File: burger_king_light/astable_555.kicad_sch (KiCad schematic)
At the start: 2 parts, among them U1 ICM7555CBAZ

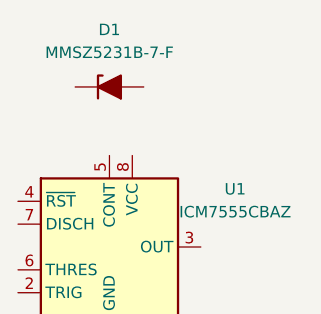
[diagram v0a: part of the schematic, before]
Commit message: changed diode designator from D1 to D2
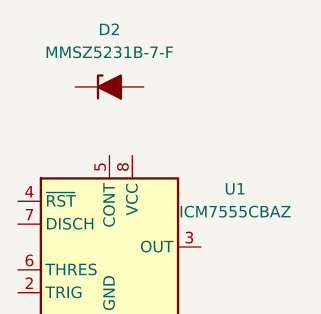
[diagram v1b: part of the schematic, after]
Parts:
- renumbered D1 to D2
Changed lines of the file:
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@@
 		(dnp no)
 		(fields_autoplaced yes)
-		(property "Reference" "D1"
+		(property "Reference" "D2"
 			(at 100.33 81.28 0)
 			(show_name no)
@@
 			(project "burger_king_light"
 				(path "/a1df17e6-efc5-454a-8f2a-f09b9061eebb/0641335a-b39f-4dc9-bc4d-328a71cdee24"
-					(reference "D1")
+					(reference "D2")
 					(unit 1)
 				)

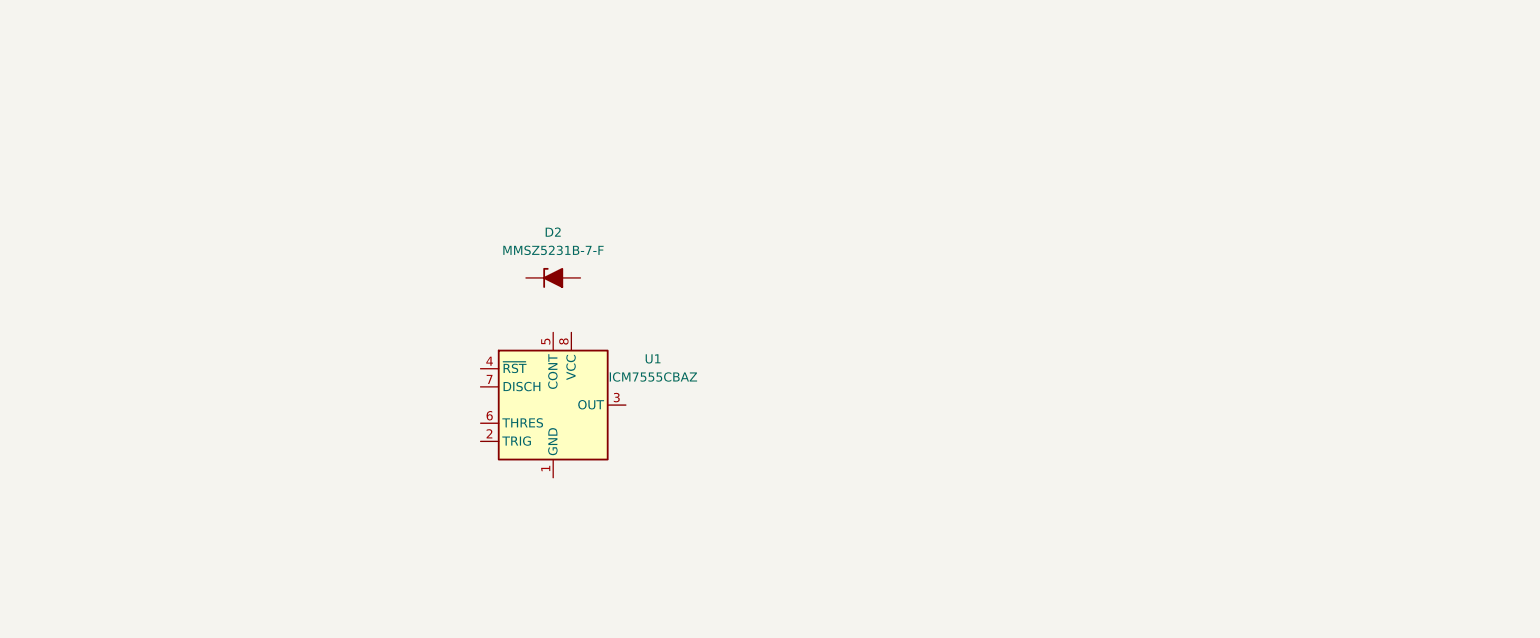
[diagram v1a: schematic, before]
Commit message: finished adding components and connections
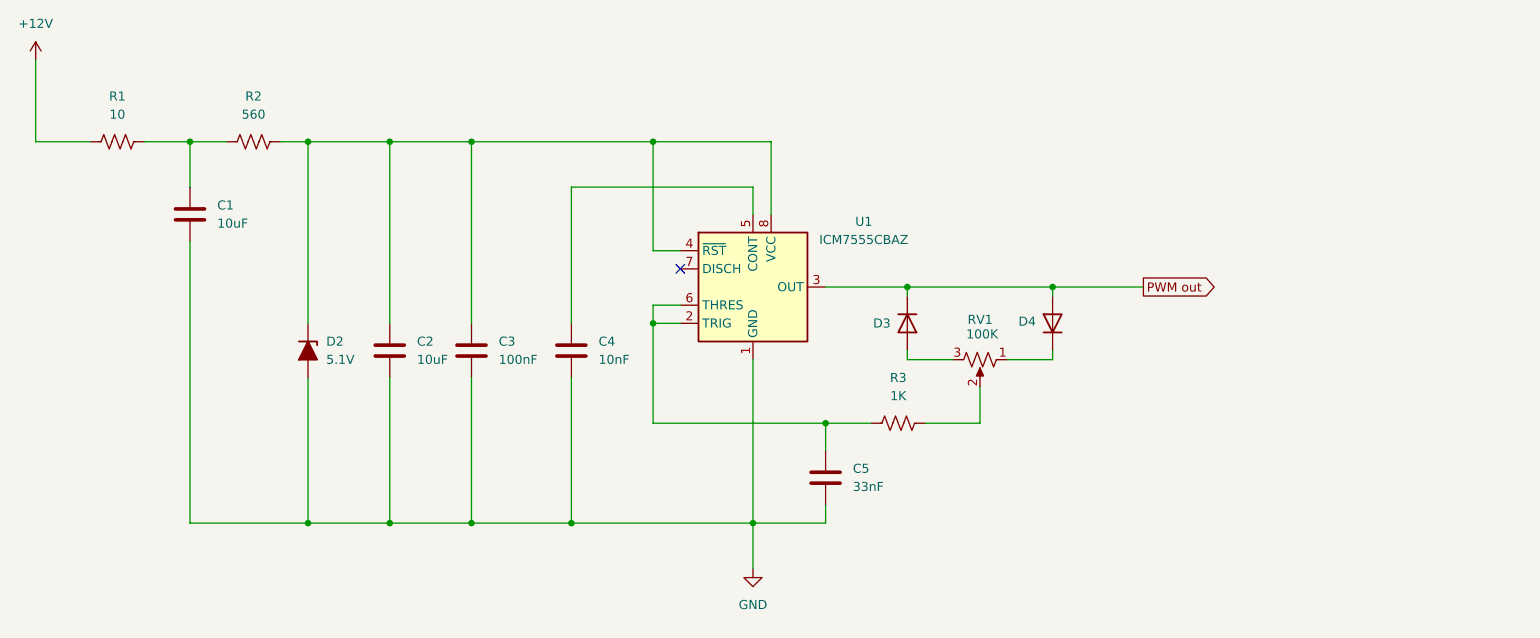
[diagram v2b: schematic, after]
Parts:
- added C1, C2: 10uF, Capacitor_SMD:C_1812_4532Metric, symbol Device:C
- added C3: 100nF, Capacitor_SMD:C_0805_2012Metric, symbol Device:C
- added C4: 10nF, Capacitor_SMD:C_1206_3216Metric, symbol Device:C
- added C5: 33nF, Capacitor_SMD:C_1206_3216Metric, symbol Device:C
- added D3, D4: 1N4148W, Diode_SMD:D_SOD-123F, symbol Diode:1N4148W
- added R1: 10, Resistor_SMD:R_1206_3216Metric, symbol Device:R_US
- added R2: 560, Resistor_SMD:R_1206_3216Metric, symbol Device:R_US
- added R3: 1K, Resistor_SMD:R_1206_3216Metric, symbol Device:R_US
- added RV1: 100K, symbol Device:R_Potentiometer_US
- D2: value MMSZ5231B-7-F -> 5.1V; Part Number (none) -> MMSZ5231B-7-F
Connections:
- net at D2.1 (K): now also U1.4 (~{RST}), U1.8 (VCC), C2.1, C3.1, R2.2
- net GND: now reaches D2.2 (A)
- net GND: now also U1.1 (GND), C1.2, C2.2, C3.2, C4.1, C5.2
- net at U1.2 (TRIG): now also U1.6 (THRES), C5.1, R3.1
- net PWM out: now reaches U1.3 (OUT)
- net PWM out: now also D3.1 (K), D4.2 (A)
- net at U1.5 (CONT): now also C4.2
- new net: D4.1 (K), RV1.1
- new net: R3.2, RV1.2
- new net: C1.1, R1.2, R2.1
- new net: D3.2 (A), RV1.3
- new net +12V: R1.1
- no-connect marks 0 -> 1
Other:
- moved on the sheet: D2, U1

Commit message: added spice models for zener and 555
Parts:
- added V1: 12, symbol Simulation_SPICE:VDC
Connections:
- net +12V: now also V1.1
- net GND renamed 0
- net 0: now also V1.2
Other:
- moved on the sheet: C1, C2, C3, C4, C5, D2, D3, D4, R1, R2, R3, RV1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
